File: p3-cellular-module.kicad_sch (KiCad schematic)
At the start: 0 parts

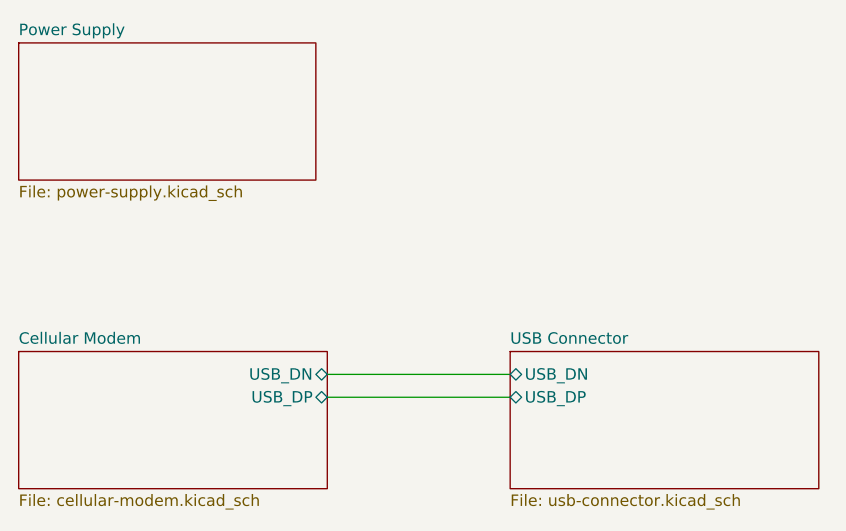
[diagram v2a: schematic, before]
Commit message: Add: Board size changes
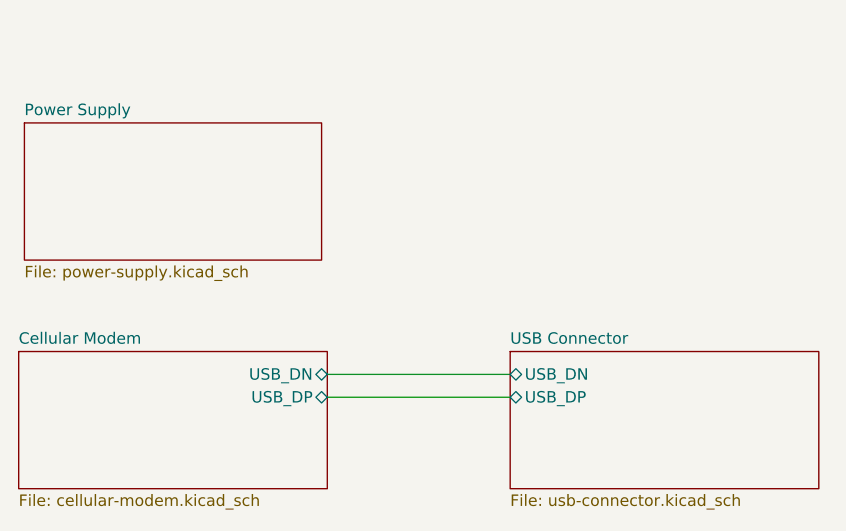
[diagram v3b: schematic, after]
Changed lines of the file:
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@@
     (stroke (width 0) (type default) (color 0 0 0 0))
   )
-  (sheet (at 106.68 72.39) (size 33.02 15.24) (fields_autoplaced)
+  (sheet (at 107.315 81.28) (size 33.02 15.24) (fields_autoplaced)
     (stroke (width 0.1524) (type solid) (color 0 0 0 0))
     (fill (color 0 0 0 0.0000))
-    (property "Sheet name" "Power Supply" (id 0) (at 106.68 71.6784 0)
+    (property "Sheet name" "Power Supply" (id 0) (at 107.315 80.5684 0)
       (effects (font (size 1.27 1.27)) (justify left bottom))
     )
-    (property "Sheet file" "power-supply.kicad_sch" (id 1) (at 106.68 88.2146 0)
+    (property "Sheet file" "power-supply.kicad_sch" (id 1) (at 107.315 97.1046 0)
       (effects (font (size 1.27 1.27)) (justify left top))
     )
